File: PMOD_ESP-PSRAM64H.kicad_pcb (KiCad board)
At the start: 2 copper layers, 21 x 18.5 mm, 4 parts, among them J1 Conn_02x06_Odd_Even, U1 ESP-PSRAM64H

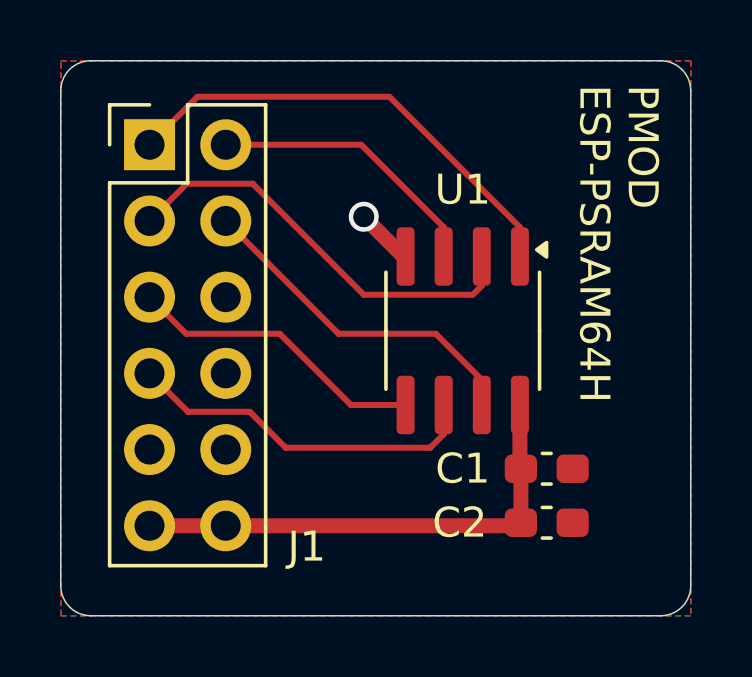
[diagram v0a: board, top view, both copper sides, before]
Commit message: fix: swap dp0, dp1 pins
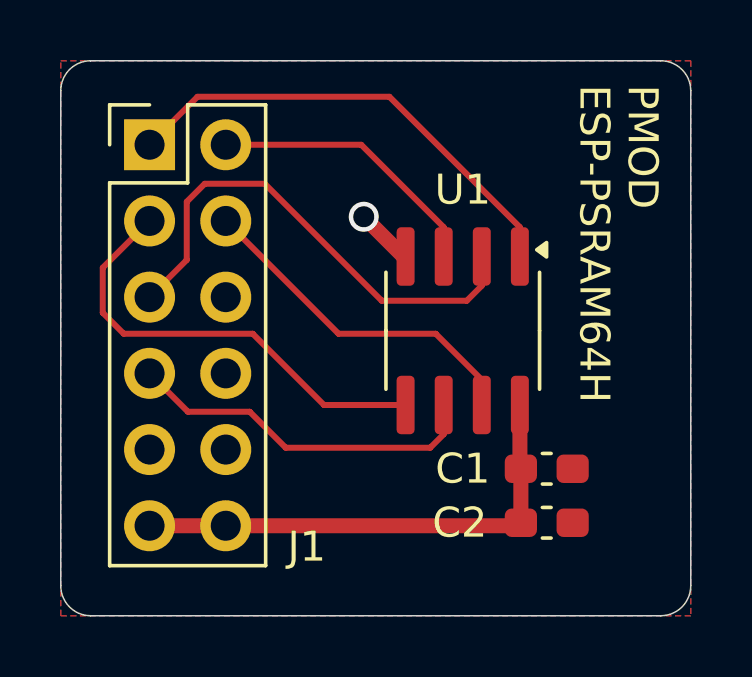
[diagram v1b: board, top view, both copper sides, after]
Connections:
- U1 pad 2: /dp0 -> /dp1
- U1 pad 5: /dp1 -> /dp0
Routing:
- net /dp1: track 10.0 -> 16.6 mm
- net /dp0: track 14.2 -> 15.1 mm
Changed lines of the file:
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@@
 		(property ki_fp_filters "C_*")
 		(sheetname "Root")
-		(sheetfile "PMOD_ESP-PSRAM32H.kicad_sch")
+		(sheetfile "PMOD_ESP-PSRAM64H.kicad_sch")
 		(attr smd)
 		(fp_line
@@
 		(property ki_fp_filters "C_*")
 		(sheetname "Root")
-		(sheetfile "PMOD_ESP-PSRAM32H.kicad_sch")
+		(sheetfile "PMOD_ESP-PSRAM64H.kicad_sch")
 		(attr smd)
 		(fp_line
@@
 		(property ki_fp_filters "SOIC*3.9x4.9mm?P1.27mm*")
 		(sheetname "Root")
-		(sheetfile "PMOD_ESP-PSRAM32H.kicad_sch")
+		(sheetfile "PMOD_ESP-PSRAM64H.kicad_sch")
 		(attr smd)
 		(fp_line
@@
 			(layers "F.Cu" "F.Paste" "F.Mask")
 			(roundrect_rratio 0.25)
-			(net 1 "/dp0")
+			(net 6 "/dp1")
 			(pinfunction "SO/SIO")
 			(pintype "output")
@@
 			(layers "F.Cu" "F.Paste" "F.Mask")
 			(roundrect_rratio 0.25)
-			(net 6 "/dp1")
+			(net 1 "/dp0")
 			(pinfunction "SI/SIO")
 			(pintype "input")
@@
 		(property ki_fp_filters "Connector*:*_2x??_*")
 		(sheetname "Root")
-		(sheetfile "PMOD_ESP-PSRAM32H.kicad_sch")
+		(sheetfile "PMOD_ESP-PSRAM64H.kicad_sch")
 		(attr through_hole)
 		(fp_line
@@
 	)
 	(segment
-		(start 139.6 77.3)
-		(end 135.9 73.6)
+		(start 131.6 78.6)
+		(end 130.9 77.9)
 		(width 0.2)
 		(layer "F.Cu")
@@
 	)
 	(segment
-		(start 135.9 73.6)
-		(end 133.7 73.6)
+		(start 130.9 77.9)
+		(end 130.9 76.4)
 		(width 0.2)
 		(layer "F.Cu")
@@
 	)
 	(segment
-		(start 143.234999 77.3)
-		(end 139.6 77.3)
+		(start 135.9 78.6)
+		(end 131.6 78.6)
 		(width 0.2)
 		(layer "F.Cu")
@@
 	)
 	(segment
-		(start 133.7 73.6)
+		(start 138.275 80.975)
+		(end 135.9 78.6)
+		(width 0.2)
+		(layer "F.Cu")
+		(net 1)
+	)
+	(segment
+		(start 130.9 76.4)
 		(end 132.46 74.84)
 		(width 0.2)
@@
 	)
 	(segment
-		(start 143.535 76.025)
-		(end 143.535 76.999999)
-		(width 0.2)
-		(layer "F.Cu")
-		(net 1)
-	)
-	(segment
-		(start 143.535 76.999999)
-		(end 143.234999 77.3)
+		(start 140.995 80.975)
+		(end 138.275 80.975)
 		(width 0.2)
 		(layer "F.Cu")
@@
 	)
 	(segment
-		(start 140.995 80.975)
-		(end 139.175 80.975)
+		(start 133.7 74.2)
+		(end 133.7 76.14)
 		(width 0.2)
 		(layer "F.Cu")
@@
 	)
 	(segment
-		(start 133.68 78.6)
+		(start 136.3 73.6)
+		(end 134.3 73.6)
+		(width 0.2)
+		(layer "F.Cu")
+		(net 6)
+	)
+	(segment
+		(start 140.2 77.5)
+		(end 136.3 73.6)
+		(width 0.2)
+		(layer "F.Cu")
+		(net 6)
+	)
+	(segment
+		(start 133.7 76.14)
 		(end 132.46 77.38)
 		(width 0.2)
@@
 	)
 	(segment
-		(start 136.8 78.6)
-		(end 133.68 78.6)
+		(start 143.535 76.999999)
+		(end 143.034999 77.5)
 		(width 0.2)
 		(layer "F.Cu")
@@
 	)
 	(segment
-		(start 139.175 80.975)
-		(end 136.8 78.6)
-		(width 0.2)
-		(layer "F.Cu")
+		(start 143.034999 77.5)
+		(end 140.2 77.5)
+		(width 0.2)
+		(layer "F.Cu")
+		(net 6)
+	)
+	(segment
+		(start 134.3 73.6)
+		(end 133.7 74.2)
+		(width 0.2)
+		(layer "F.Cu")
+		(net 6)
+	)
+	(segment
+		(start 143.535 76.025)
+		(end 143.535 76.999999)
+		(width 0.2)
+		(layer "F.Cu")
